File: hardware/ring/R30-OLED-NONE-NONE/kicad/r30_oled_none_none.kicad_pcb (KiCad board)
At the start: 2 copper layers, 42 x 18 mm, 27 parts, among them J1 USB4215-class 16P TH stakes, Q1 SI2301 P-FET, Q2 2N7002 gate driver, SW1 5mm 200gf dome, U1 ESP32-C3-MINI-1-N4, U2 PAW3204DB-TJ3L, U3 TP4054, U4 RT9080-33GJ5

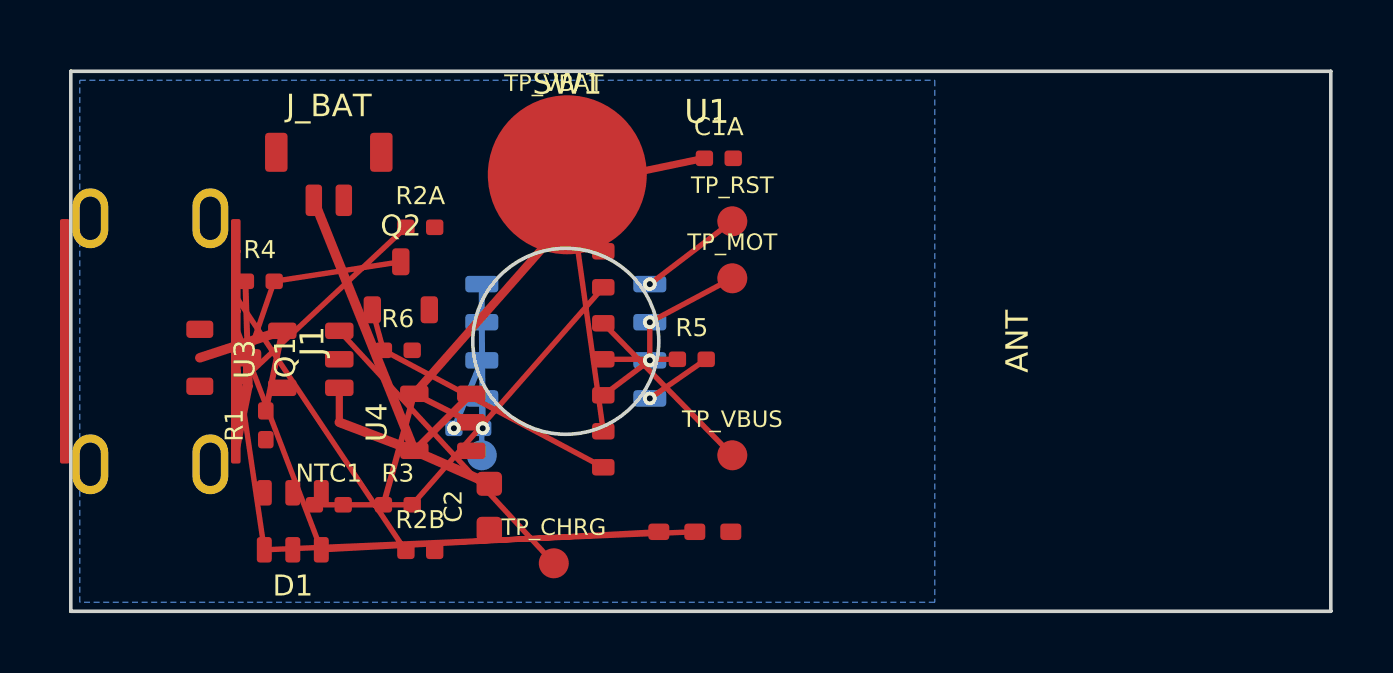
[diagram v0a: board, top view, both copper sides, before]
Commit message: feat(hardware): lock R30 sense and schematic baseline
Design disclosure: sensing mechanism PAW3204-class optical tracking; form factor R30-OLED-NONE-NONE fingertip ring, active 30-degree ring packet; intended use BLE HID pointing for accessibility; BOM estimate ~$5.30-9.45.

Record the accepted 2N7002 charge-gate path, R7-R11 sense/status values, current KiCad red baseline, and directly linked packet truth docs.
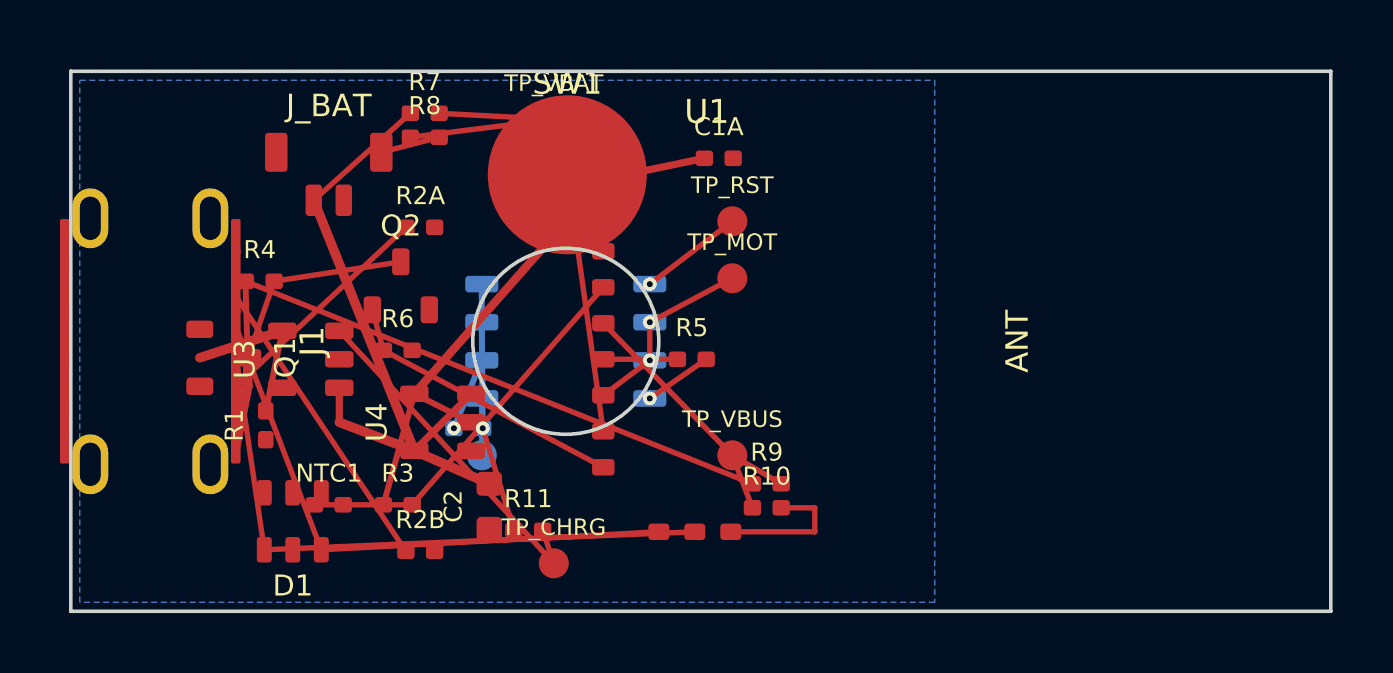
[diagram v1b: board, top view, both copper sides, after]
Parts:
- added R10: 100k, Resistor_SMD:R_0402_1005Metric, F.Cu at (123.2, 105.5)
- added R11: 100k, Resistor_SMD:R_0402_1005Metric, F.Cu at (115.2, 106.3)
- added R7: 100k, Resistor_SMD:R_0402_1005Metric, F.Cu at (111.8, 92.4)
- added R8: 100k, Resistor_SMD:R_0402_1005Metric, F.Cu at (111.8, 93.2)
- added R9: 220k, Resistor_SMD:R_0402_1005Metric, F.Cu at (123.2, 104.8)
- TP_CHRG: value CHRG_STAT bring-up only -> CHRG_STAT pulled-up status pad
- TP_VBAT: value VBAT sense divider not yet in BOM -> VBAT_SENSE after R7/R8 divider
- TP_VBUS: value VBUS detect divider not yet in BOM -> VBUS_DETECT after R9/R10 divider
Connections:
- net VBAT_SENSE_TP renamed VBAT_SENSE
- net VBUS_DETECT_TP renamed VBUS_DETECT
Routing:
- net VBUS_5V: track 5.54 -> 23.7 mm
- net VBAT_SENSE: track 4.70 -> 13.3 mm
- net GND: track 2.45 -> 9.16 mm
- net VBAT_PROTECTED: track 18.2 -> 22.6 mm
- net VBUS_DETECT: track 6.15 -> 9.91 mm
- net VREG_3V3: track 24.2 -> 27.7 mm
- net CHRG_STAT: track 10.5 -> 11.7 mm

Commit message: fix(r30): clean schematic erc library baseline
Design disclosure: sensing mechanism PAW3204-class optical tracking; form factor R30-OLED-NONE-NONE fingertip ring, active 30-degree ring packet; intended use BLE HID pointing for accessibility; BOM estimate ~$5.30-9.45.

Materialize the project-local PowerFinger symbol and PowerFinger_Ring footprint libraries, wire sheet-interface labels, keep PAW3204 reset/motion local to sensor test pads, and update the verified KiCad snapshot to ERC=0, DRC=349, unconnected=41, parity=118.
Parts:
- NTC1: footprint Device:Thermistor_NTC_0402_1005Metric -> PowerFinger_Ring:Thermistor_NTC_0402_1005Metric
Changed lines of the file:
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@@
     (pad "2" smd roundrect (at 0.48 0) (size 0.58 0.52) (layers "F.Cu" "F.Paste" "F.Mask") (roundrect_rratio 0.20) (net 9 "NTC_SENSE") (pinfunction "2") (pintype "passive"))
   )
-  (footprint "Device:Thermistor_NTC_0402_1005Metric"
+  (footprint "PowerFinger_Ring:Thermistor_NTC_0402_1005Metric"
     (layer "F.Cu")
     (at 108.600 105.450 0)

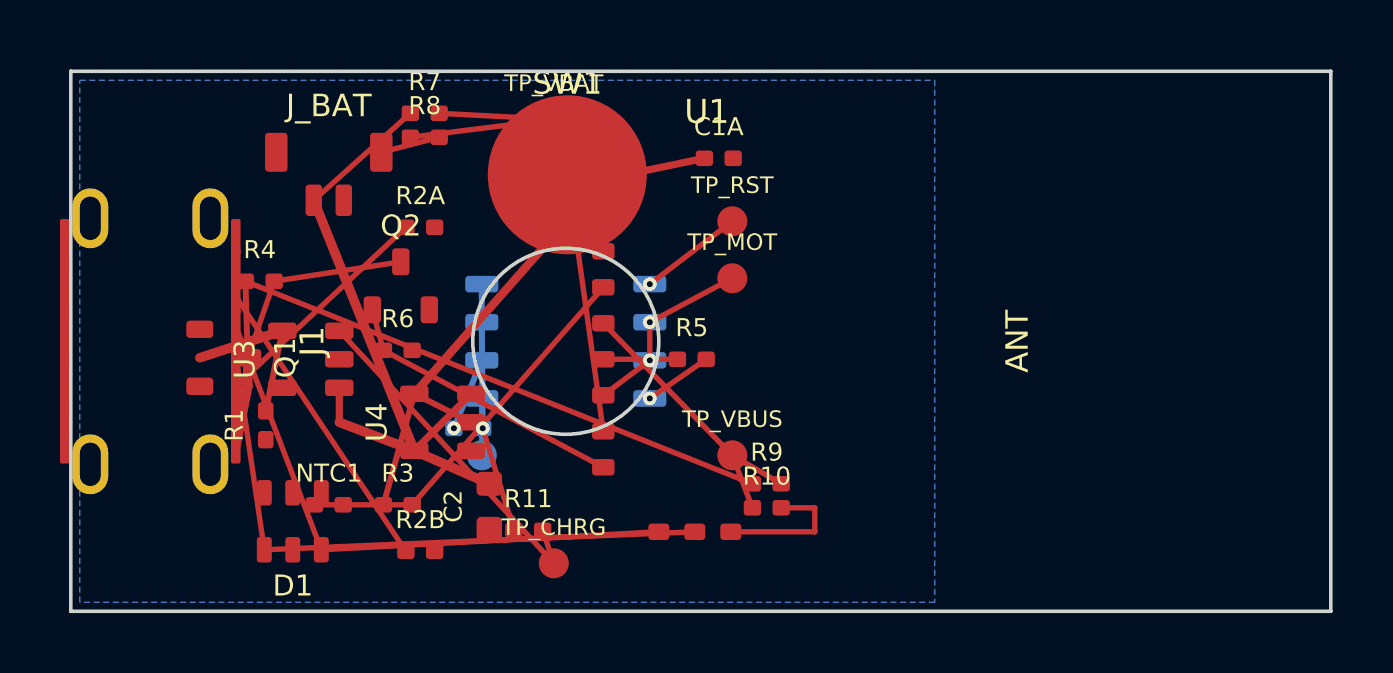
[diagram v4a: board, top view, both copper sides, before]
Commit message: fix(r30): reduce first routing drc blockers
Sensing mechanism: PAW3204 optical surface tracking.

Form factor and angle: R30 30-degree ring, OLED/NONE/NONE active lane.

Intended use: accessibility-first BLE HID pointing first-board validation.

BOM estimate: active R30 prototype remains about $5.30-$9.45, target about $9.
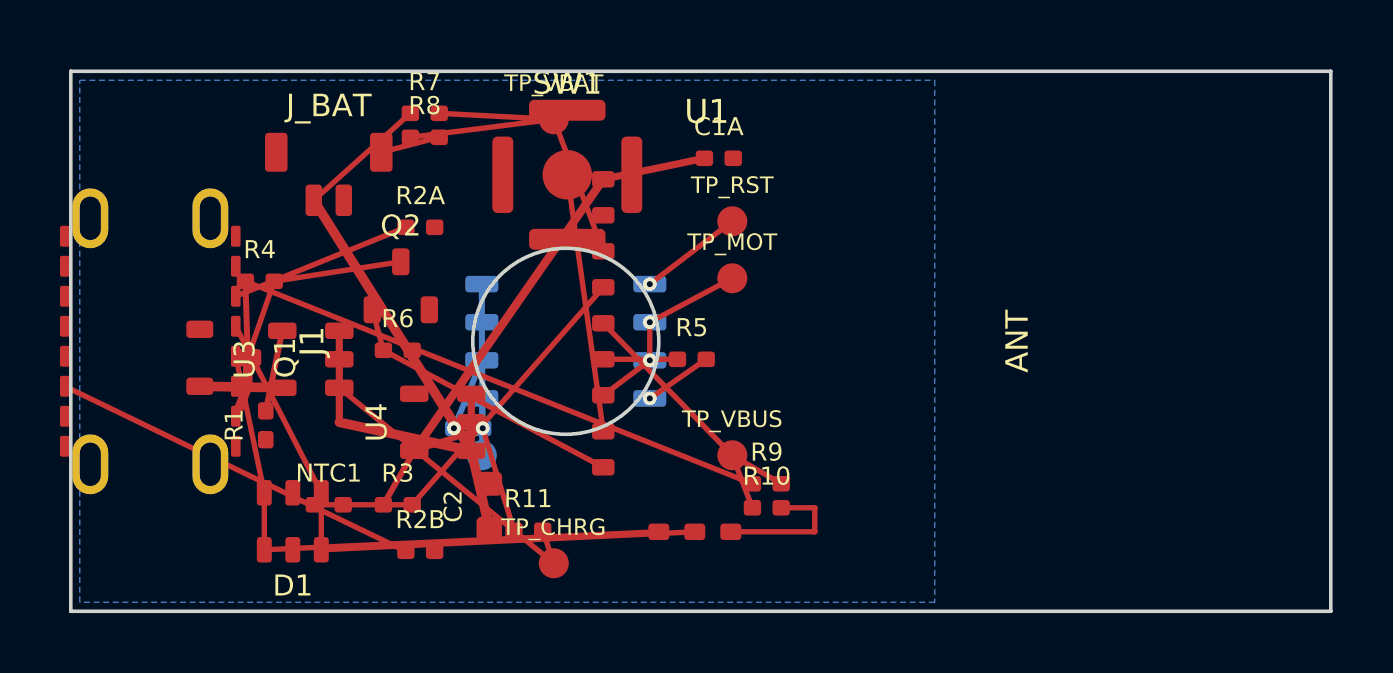
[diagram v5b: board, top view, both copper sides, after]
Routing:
- net VBAT_PROTECTED: track 22.6 -> 26.3 mm
- net USB_CC2_RD: track 10.2 -> 12.6 mm
- net USB_CC1_RD: track 7.76 -> 6.12 mm
- net CHRG_STAT: track 11.7 -> 10.4 mm
- net VBUS_5V: track 23.7 -> 22.8 mm

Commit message: fix(r30): cut routing drc blockers
Sensing mechanism: PAW3204 optical surface tracking.

Form factor and angle: R30 30-degree ring, OLED/NONE/NONE active lane.

Intended use: accessibility-first BLE HID pointing first-board validation.

BOM estimate: active R30 prototype remains about $5.30-$9.45, target about $9.
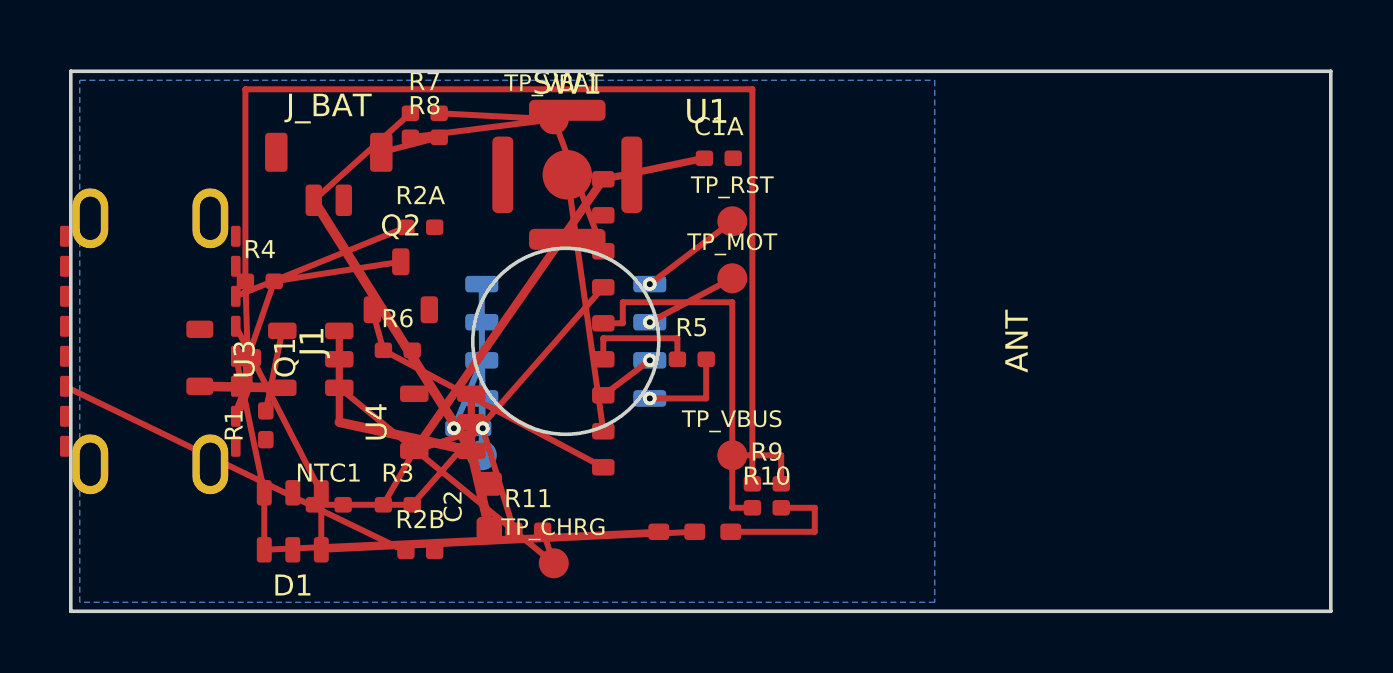
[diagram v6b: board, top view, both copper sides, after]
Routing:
- net VBUS_5V: track 22.8 -> 41.0 mm
- net VBUS_DETECT: track 9.91 -> 15.1 mm
- net SENSOR_SCLK: track 2.47 -> 3.87 mm
- net SENSOR_SDIO: track 3.21 -> 1.94 mm
- net SENSOR_SCLK_DAMPED: track 2.29 -> 3.19 mm
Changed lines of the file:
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@@
   (segment (start 112.770 102.900) (end 113.700 100.635) (width 0.20) (layer "B.Cu") (net 1))
   (segment (start 107.050 99.650) (end 106.500 102.320) (width 0.20) (layer "F.Cu") (net 6))
-  (segment (start 105.900 100.550) (end 106.780 98.000) (width 0.18) (layer "F.Cu") (net 7))
-  (segment (start 106.780 98.000) (end 111.000 97.350) (width 0.18) (layer "F.Cu") (net 7))
-  (segment (start 110.050 98.950) (end 110.420 100.300) (width 0.18) (layer "F.Cu") (net 8))
-  (segment (start 110.420 100.300) (end 117.750 104.200) (width 0.18) (layer "F.Cu") (net 8))
-  (segment (start 111.320 92.400) (end 108.100 95.300) (width 0.18) (layer "F.Cu") (net 4))
-  (segment (start 112.280 93.200) (end 110.350 93.700) (width 0.18) (layer "F.Cu") (net 1))
-  (segment (start 122.720 104.750) (end 105.820 98.000) (width 0.18) (layer "F.Cu") (net 2))
-  (segment (start 123.680 105.550) (end 124.800 105.550) (width 0.18) (layer "F.Cu") (net 1))
-  (segment (start 124.800 105.550) (end 124.800 106.350) (width 0.18) (layer "F.Cu") (net 1))
-  (segment (start 124.800 106.350) (end 122.000 106.350) (width 0.18) (layer "F.Cu") (net 1))
-  (segment (start 114.770 106.300) (end 113.730 102.900) (width 0.18) (layer "F.Cu") (net 5))
-  (segment (start 115.730 106.300) (end 116.100 107.400) (width 0.18) (layer "F.Cu") (net 20))
-  (segment (start 108.120 105.450) (end 111.380 105.450) (width 0.18) (layer "F.Cu") (net 9))
-  (segment (start 111.380 105.450) (end 117.750 98.200) (width 0.18) (layer "F.Cu") (net 9))
-  (segment (start 117.750 100.600) (end 120.220 100.600) (width 0.18) (layer "F.Cu") (net 10))
-  (segment (start 121.180 100.600) (end 119.300 101.905) (width 0.18) (layer "F.Cu") (net 11))
-  (segment (start 117.750 101.800) (end 119.300 100.635) (width 0.18) (layer "F.Cu") (net 12))
-  (segment (start 119.300 100.635) (end 119.300 99.365) (width 0.18) (layer "F.Cu") (net 12))
-  (segment (start 119.300 99.365) (end 122.050 97.900) (width 0.18) (layer "F.Cu") (net 13))
-  (segment (start 119.300 98.095) (end 122.050 96.000) (width 0.18) (layer "F.Cu") (net 14))
-  (segment (start 117.750 103.000) (end 116.550 94.450) (width 0.18) (layer "F.Cu") (net 15))
-  (segment (start 105.500 99.500) (end 108.350 105.050) (width 0.18) (layer "F.Cu") (net 16))
-  (segment (start 108.350 106.950) (end 120.800 106.350) (width 0.18) (layer "F.Cu") (net 16))
-  (segment (start 108.350 105.050) (end 108.350 106.950) (width 0.18) (layer "F.Cu") (net 16))
-  (segment (start 105.500 100.500) (end 106.450 105.050) (width 0.18) (layer "F.Cu") (net 17))
-  (segment (start 106.450 106.950) (end 119.600 106.350) (width 0.18) (layer "F.Cu") (net 17))
-  (segment (start 106.450 105.050) (end 106.450 106.950) (width 0.18) (layer "F.Cu") (net 17))
-  (segment (start 105.500 98.500) (end 111.170 96.200) (width 0.18) (layer "F.Cu") (net 18))
-  (segment (start 99.800 101.500) (end 111.170 107.000) (width 0.18) (layer "F.Cu") (net 19))
-  (segment (start 108.950 101.550) (end 116.100 107.400) (width 0.18) (layer "F.Cu") (net 20))
-  (segment (start 116.100 92.600) (end 117.750 97.000) (width 0.18) (layer "F.Cu") (net 21))
-  (segment (start 112.280 92.400) (end 116.100 92.600) (width 0.18) (layer "F.Cu") (net 21))
-  (segment (start 111.320 93.200) (end 116.100 92.600) (width 0.18) (layer "F.Cu") (net 21))
-  (segment (start 122.050 103.800) (end 117.750 99.400) (width 0.18) (layer "F.Cu") (net 22))
-  (segment (start 123.680 104.750) (end 122.050 103.800) (width 0.18) (layer "F.Cu") (net 22))
-  (segment (start 122.720 105.550) (end 122.050 103.800) (width 0.18) (layer "F.Cu") (net 22))
-  (segment (start 113.700 101.905) (end 113.700 103.800) (width 0.18) (layer "B.Cu") (net 23))
+  (segment (start 105.900 100.550) (end 106.780 98.000) (width 0.20) (layer "F.Cu") (net 7))
+  (segment (start 106.780 98.000) (end 111.000 97.350) (width 0.20) (layer "F.Cu") (net 7))
+  (segment (start 110.050 98.950) (end 110.420 100.300) (width 0.20) (layer "F.Cu") (net 8))
+  (segment (start 110.420 100.300) (end 117.750 104.200) (width 0.20) (layer "F.Cu") (net 8))
+  (segment (start 111.320 92.400) (end 108.100 95.300) (width 0.20) (layer "F.Cu") (net 4))
+  (segment (start 112.280 93.200) (end 110.350 93.700) (width 0.20) (layer "F.Cu") (net 1))
+  (segment (start 105.820 98.000) (end 105.820 91.600) (width 0.20) (layer "F.Cu") (net 2))
+  (segment (start 105.820 91.600) (end 122.720 91.600) (width 0.20) (layer "F.Cu") (net 2))
+  (segment (start 122.720 91.600) (end 122.720 104.750) (width 0.20) (layer "F.Cu") (net 2))
+  (segment (start 123.680 105.550) (end 124.800 105.550) (width 0.20) (layer "F.Cu") (net 1))
+  (segment (start 124.800 105.550) (end 124.800 106.350) (width 0.20) (layer "F.Cu") (net 1))
+  (segment (start 124.800 106.350) (end 122.000 106.350) (width 0.20) (layer "F.Cu") (net 1))
+  (segment (start 114.770 106.300) (end 113.730 102.900) (width 0.20) (layer "F.Cu") (net 5))
+  (segment (start 115.730 106.300) (end 116.100 107.400) (width 0.20) (layer "F.Cu") (net 20))
+  (segment (start 108.120 105.450) (end 111.380 105.450) (width 0.20) (layer "F.Cu") (net 9))
+  (segment (start 111.380 105.450) (end 117.750 98.200) (width 0.20) (layer "F.Cu") (net 9))
+  (segment (start 117.750 100.600) (end 117.750 99.900) (width 0.20) (layer "F.Cu") (net 10))
+  (segment (start 117.750 99.900) (end 120.220 99.900) (width 0.20) (layer "F.Cu") (net 10))
+  (segment (start 120.220 99.900) (end 120.220 100.600) (width 0.20) (layer "F.Cu") (net 10))
+  (segment (start 121.180 100.600) (end 121.180 101.905) (width 0.20) (layer "F.Cu") (net 11))
+  (segment (start 121.180 101.905) (end 119.300 101.905) (width 0.20) (layer "F.Cu") (net 11))
+  (segment (start 117.750 101.800) (end 119.300 100.635) (width 0.20) (layer "F.Cu") (net 12))
+  (segment (start 119.300 99.365) (end 122.050 97.900) (width 0.20) (layer "F.Cu") (net 13))
+  (segment (start 119.300 98.095) (end 122.050 96.000) (width 0.20) (layer "F.Cu") (net 14))
+  (segment (start 117.750 103.000) (end 116.550 94.450) (width 0.20) (layer "F.Cu") (net 15))
+  (segment (start 105.500 99.500) (end 108.350 105.050) (width 0.20) (layer "F.Cu") (net 16))
+  (segment (start 108.350 106.950) (end 120.800 106.350) (width 0.20) (layer "F.Cu") (net 16))
+  (segment (start 108.350 105.050) (end 108.350 106.950) (width 0.20) (layer "F.Cu") (net 16))
+  (segment (start 105.500 100.500) (end 106.450 105.050) (width 0.20) (layer "F.Cu") (net 17))
+  (segment (start 106.450 106.950) (end 119.600 106.350) (width 0.20) (layer "F.Cu") (net 17))
+  (segment (start 106.450 105.050) (end 106.450 106.950) (width 0.20) (layer "F.Cu") (net 17))
+  (segment (start 105.500 98.500) (end 111.170 96.200) (width 0.20) (layer "F.Cu") (net 18))
+  (segment (start 99.800 101.500) (end 111.170 107.000) (width 0.20) (layer "F.Cu") (net 19))
+  (segment (start 108.950 101.550) (end 116.100 107.400) (width 0.20) (layer "F.Cu") (net 20))
+  (segment (start 116.100 92.600) (end 117.750 97.000) (width 0.20) (layer "F.Cu") (net 21))
+  (segment (start 112.280 92.400) (end 116.100 92.600) (width 0.20) (layer "F.Cu") (net 21))
+  (segment (start 111.320 93.200) (end 116.100 92.600) (width 0.20) (layer "F.Cu") (net 21))
+  (segment (start 117.750 99.400) (end 118.400 99.400) (width 0.20) (layer "F.Cu") (net 22))
+  (segment (start 118.400 99.400) (end 118.400 98.700) (width 0.20) (layer "F.Cu") (net 22))
+  (segment (start 118.400 98.700) (end 122.050 98.700) (width 0.20) (layer "F.Cu") (net 22))
+  (segment (start 122.050 98.700) (end 122.050 103.800) (width 0.20) (layer "F.Cu") (net 22))
+  (segment (start 123.680 104.750) (end 123.680 103.800) (width 0.20) (layer "F.Cu") (net 22))
+  (segment (start 123.680 103.800) (end 122.050 103.800) (width 0.20) (layer "F.Cu") (net 22))
+  (segment (start 122.720 105.550) (end 122.050 105.550) (width 0.20) (layer "F.Cu") (net 22))
+  (segment (start 122.050 105.550) (end 122.050 103.800) (width 0.20) (layer "F.Cu") (net 22))
+  (segment (start 113.700 101.905) (end 113.700 103.800) (width 0.20) (layer "B.Cu") (net 23))
   (via (at 113.730 102.900) (size 0.46) (drill 0.20) (layers "F.Cu" "B.Cu") (net 5))
   (via (at 112.770 102.900) (size 0.46) (drill 0.20) (layers "F.Cu" "B.Cu") (net 1))
